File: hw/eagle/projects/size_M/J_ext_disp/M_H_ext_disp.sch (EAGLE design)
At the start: 18 parts, among them U1 CP2104-F03-GM

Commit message: pcb M.1 -not finished
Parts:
- removed C.C1, C.C2, C.C4: 100n, rcl:C-EUC0603
- removed C.C3: 22u, rcl:C-EUC0805
- removed C.C5: 10u, rcl:C-EUC0603
- removed C.C6: 2u2, rcl:C-EUC0603
- removed C.J2: (no value), pinhead2:PINHD-1X6
- removed C.R1, C.R2: 2k2, rcl:R-EU_R0603
- removed C.R3, C.R4, C.R5, C.R6: 12k, rcl:R-EU_R0603
- removed C.U1: TTGO-MICRO-32, hugo:TTGO-MICRO-32
- removed C.U3: BC817DS,115, SamacSys_Parts:BC817DS,115
- removed U$1: USB-C, hugo:USB-C
- removed U1: CP2104-F03-GM, CP2104:CP2104-F03-GM
- added C1, C4: 1u, rcl:C-EUC0603
- added C2, C5: 2u2, rcl:C-EUC0603
- added C3: 2u, rcl:C-EUC0603
- added C6: 100n, rcl:C-EUC0603
- added J1: SSD_1306_STM32_OLED, hugo:SSD_1306_STM32_OLED
- added JP2: (no value), pinhead2:PINHD-1X2
- added R1: 390, rcl:R-EU_R0603
- added R2: 100k, rcl:R-EU_R0603
- JP1: device pinhead2:PINHD-1X4 -> pinhead2:PINHD-1X3
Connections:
- removed net N$11: C.C6.1, C.R6.2, C.U1.EN, C.U3.COLLECTOR_2
- removed net N$13: C.U1.IO2
- removed net N$2: U$1.D1_P, U1.DP
- removed net RX: C.U1.RXD0, U1.RXD
- removed net TX: C.U1.TXD0, U1.TXD
- removed net VCC: C.C1.1, C.C2.1, C.C3.1, C.R1.2, C.R2.2, C.R5.2, C.R6.1, C.U1.3V3, JP1.3, U1.VDD
- removed net VUSB: C.C4.2, C.C5.2, JP1.2, U$1.VBUS1, U$1.VBUS2, U1.REGIN, U1.VBUS
- new net N$3: C3.2, J1.VCC
- new net PA7: J1.DC#/I2C_A0, JP1.3, R2.1
- new net VDD: C5.2, C6.2, J1.BS1, J1.RES#, J1.VBAT, J1.VDD, JP2.1, R2.2
- net GND: now also C2.1, C3.1, C5.1, C6.1, J1.BS2, J1.CS#, J1.D3, J1.D4, J1.D5, J1.D6, J1.D7, J1.E/RD#, J1.NC(GND)$1, J1.NC(GND)$2, J1.R/W#, J1.VLSS, J1.VSS, JP2.2, R1.1; no longer C.C1.2, C.C2.2, C.C3.2, C.C4.1, C.C5.1, C.C6.2, C.J2.6, C.U1.GND, C.U1.GND2, C.U1.GND3, JP1.4, U$1.GND1, U$1.GND2, U1.GND
- net N$1: now also J1.IREF, R1.2; no longer U$1.D1_N, U1.DN
- net N$10: now also C4.1, J1.C1N; no longer C.R5.1, C.U1.IO0, C.U3.COLLECTOR_1
- net N$5: now also C2.2, J1.VCOMH; no longer C.R4.2, C.U3.BASE_2
- net N$7: now also C1.2, J1.C2P; no longer C.R3.2, C.U3.BASE_1
- net N$8: now also C1.1, J1.C2N; no longer C.R3.1, C.U3.EMITTER_2, U1.!RTS
- net N$9: now also C4.2, J1.C1P; no longer C.R4.1, C.U3.EMITTER_1, U1.!DTR
- net SCL: now also J1.D0/I2C_SCL, JP1.1; no longer C.J2.1, C.R1.1, C.U1.IO22
- net SDA: now also J1.D1/I2C_SDA, J1.D2/I2C_SDA, JP1.2; no longer C.J2.2, C.R2.1, C.U1.IO21

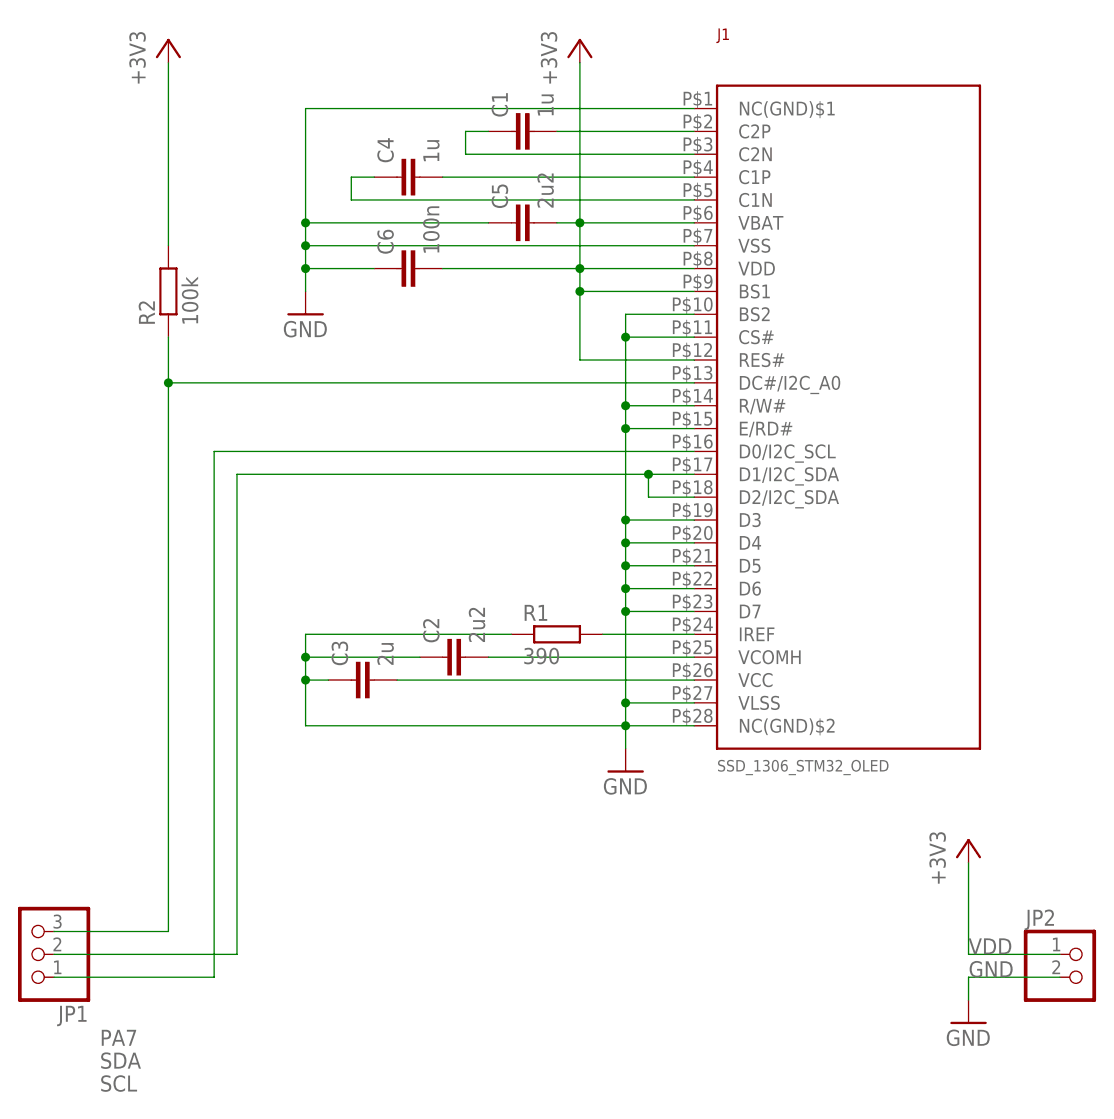
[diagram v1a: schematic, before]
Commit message: updateed PCBs - adjustments based on usage of version 1
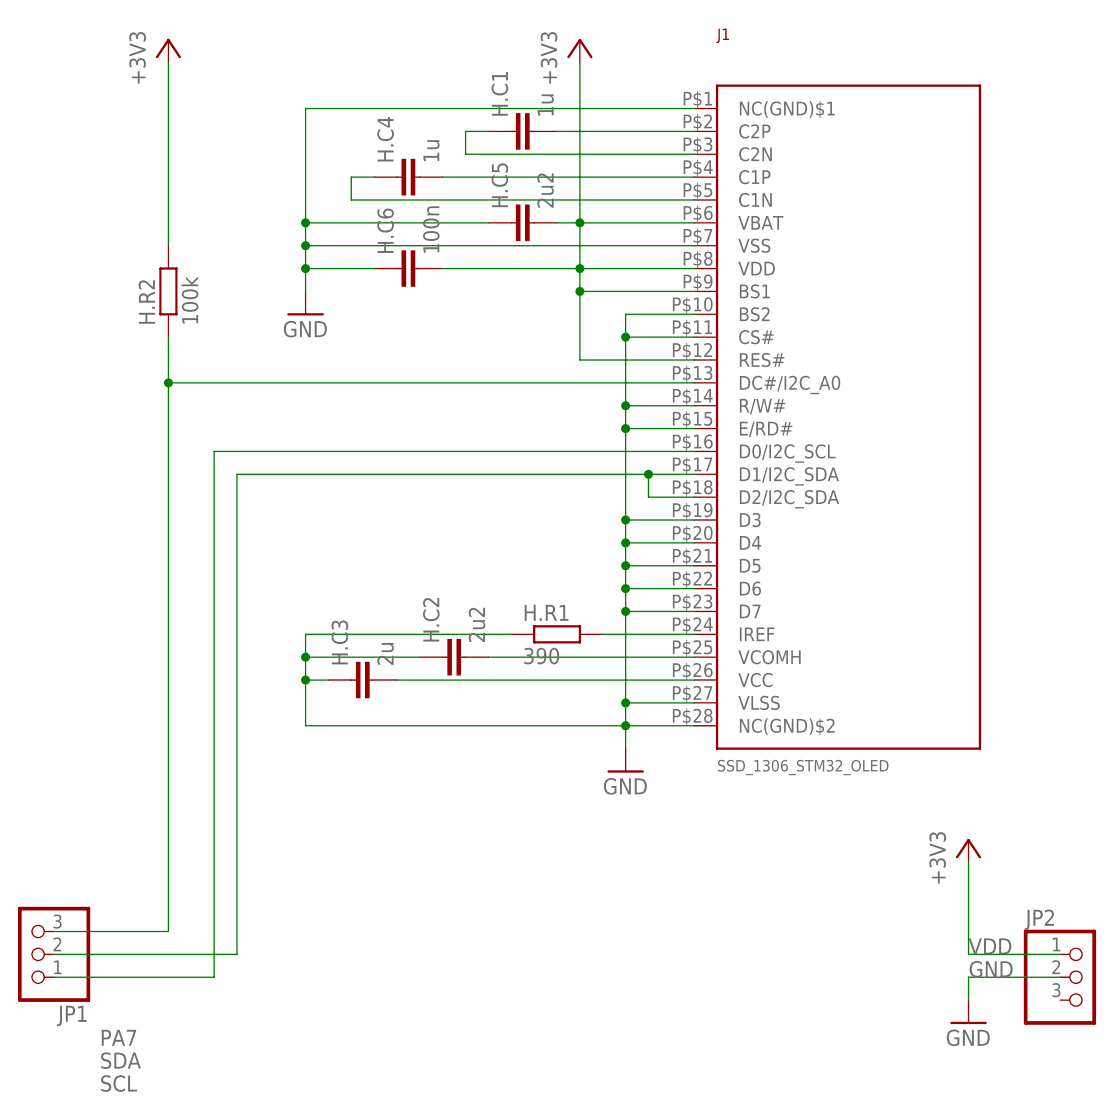
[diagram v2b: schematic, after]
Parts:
- JP2: device pinhead2:PINHD-1X2 -> pinhead2:PINHD-1X3
- renumbered C1 to H.C1, C2 to H.C2, C3 to H.C3, C4 to H.C4, C5 to H.C5, C6 to H.C6, R1 to H.R1, R2 to H.R2
